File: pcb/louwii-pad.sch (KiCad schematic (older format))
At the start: 50 parts, among them J1 USB_B_Micro, J2 ICSP, J3 IIC, K1 KEYSW, K2 KEYSW, K3 KEYSW, K4 KEYSW, K5 KEYSW, K6 KEYSW, K7 KEYSW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

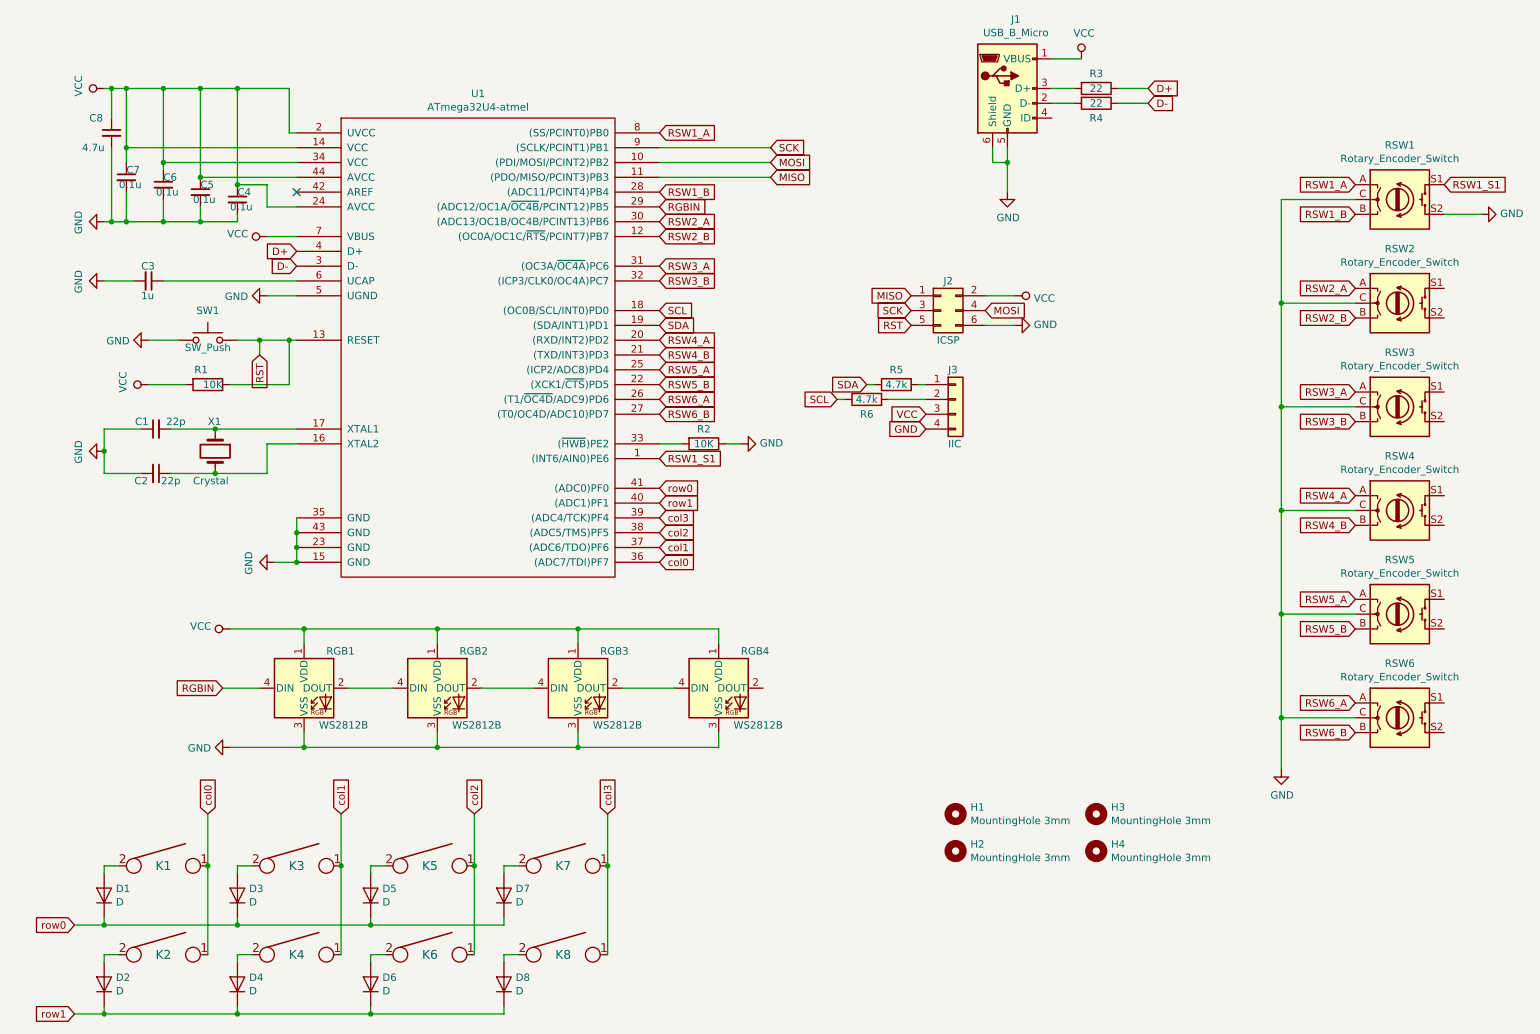
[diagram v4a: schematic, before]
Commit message: update schematics, update net, update footprints, update pcb design with missing footprints
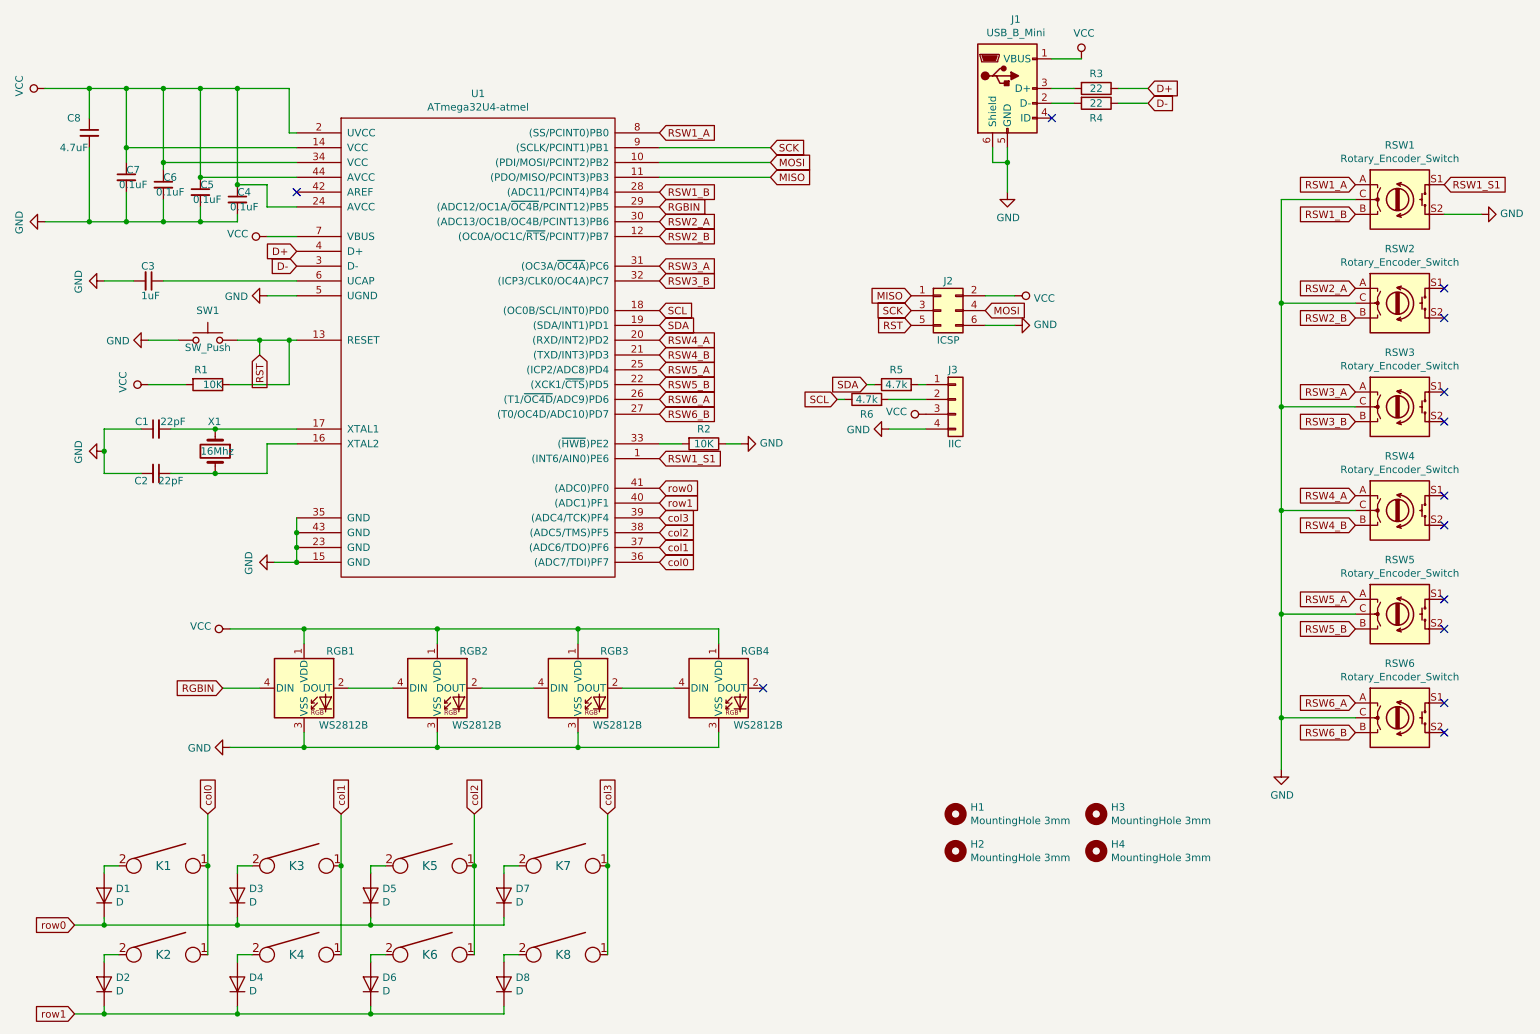
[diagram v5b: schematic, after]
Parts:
- removed J1: USB_B_Micro, Connector_USB:USB_Micro-B_Wuerth_629105150521, symbol Connector:USB_B_Micro
- added J1: USB_B_Mini, Connector_USB:USB_Mini-B_Lumberg_2486_01_Horizontal, symbol Connector:USB_B_Mini
- C1, C2: value 22p -> 22pF; footprint (none) -> Capacitor_THT:C_Disc_D4.3mm_W1.9mm_P5.00mm
- C3: value 1u -> 1uF; footprint (none) -> Capacitor_THT:C_Disc_D4.3mm_W1.9mm_P5.00mm
- C4, C5, C6, C7: value 0.1u -> 0.1uF; footprint (none) -> Capacitor_THT:C_Disc_D4.3mm_W1.9mm_P5.00mm
- C8: value 4.7u -> 4.7uF; footprint (none) -> Capacitor_THT:C_Radial_D5.0mm_H7.0mm_P2.00mm
- H1, H2, H3, H4: footprint (none) -> MountingHole:MountingHole_3.2mm_M3_ISO7380_Pad
- SW1: footprint (none) -> Button_Switch_SMD:SW_SPST_TL3342
- X1: value Crystal -> 16Mhz
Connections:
- net GND: now also J1.5 (GND), J1.6 (Shield)
- net VCC: now also J1.1 (VBUS)
- net at R4.2: now also J1.2 (D-)
- net at R3.2: now also J1.3 (D+)
- no-connect marks 1 -> 13
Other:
- moved on the sheet: C8
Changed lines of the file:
@@
 P 2050 3650
 F 0 "X1" V 1850 3600 50  0000 L CNN
-F 1 "Crystal" V 2250 3500 50  0000 L CNN
+F 1 "16Mhz" V 2050 3550 50  0000 L CNN
 F 2 "Crystal:Crystal_HC49-U_Vertical" H 2050 3650 50  0001 C CNN
 F 3 "~" H 2050 3650 50  0001 C CNN
@@
 P 1650 3800
 F 0 "C2" V 1700 3700 50  0000 C CNN
-F 1 "22p" V 1700 3900 50  0000 C CNN
-F 2 "" H 1650 3800 50  0001 C CNN
+F 1 "22pF" V 1700 3900 50  0000 C CNN
+F 2 "Capacitor_THT:C_Disc_D4.3mm_W1.9mm_P5.00mm" H 1650 3800 50  0001 C CNN
 F 3 "~" H 1650 3800 50  0001 C CNN
 	1    1650 3800
@@
 P 1650 3500
 F 0 "C1" V 1700 3550 50  0000 L CNN
-F 1 "22p" V 1700 3300 50  0000 L CNN
-F 2 "" H 1650 3500 50  0001 C CNN
+F 1 "22pF" V 1700 3300 50  0000 L CNN
+F 2 "Capacitor_THT:C_Disc_D4.3mm_W1.9mm_P5.00mm" H 1650 3500 50  0001 C CNN
 F 3 "~" H 1650 3500 50  0001 C CNN
 	1    1650 3500
 	0    -1   -1   0
-$EndComp
-$Comp
-L Connector:USB_B_Micro J1
-U 1 1 5DB104A8
-P 7400 1200
-F 0 "J1" H 7457 1667 50  0000 C CNN
-F 1 "USB_B_Micro" H 7457 1576 50  0000 C CNN
-F 2 "Connector_USB:USB_Micro-B_Wuerth_629105150521" H 7550 1150 50  0001 C CNN
-F 3 "~" H 7550 1150 50  0001 C CNN
-	1    7400 1200
-	1    0    0    -1
 $EndComp
 $Comp
@@
 P 1600 2500
 F 0 "C3" V 1500 2450 50  0000 L CNN
-F 1 "1u" V 1700 2450 50  0000 L CNN
-F 2 "" H 1600 2500 50  0001 C CNN
+F 1 "1uF" V 1700 2450 50  0000 L CNN
+F 2 "Capacitor_THT:C_Disc_D4.3mm_W1.9mm_P5.00mm" H 1600 2500 50  0001 C CNN
 F 3 "~" H 1600 2500 50  0001 C CNN
 	1    1600 2500
@@
 F 0 "SW1" H 2000 3100 50  0000 C CNN
 F 1 "SW_Push" H 2000 2850 50  0000 C CNN
-F 2 "" H 2000 3100 50  0001 C CNN
+F 2 "Button_Switch_SMD:SW_SPST_TL3342" H 2000 3100 50  0001 C CNN
 F 3 "~" H 2000 3100 50  0001 C CNN
 	1    2000 2900
@@
 P 2200 1950
 F 0 "C4" H 2200 2000 50  0000 L CNN
-F 1 "0.1u" H 2150 1900 50  0000 L CNN
-F 2 "" H 2200 1950 50  0001 C CNN
+F 1 "0.1uF" H 2150 1900 50  0000 L CNN
+F 2 "Capacitor_THT:C_Disc_D4.3mm_W1.9mm_P5.00mm" H 2200 1950 50  0001 C CNN
 F 3 "~" H 2200 1950 50  0001 C CNN
 	1    2200 1950
@@
 P 1950 1900
 F 0 "C5" H 1950 1950 50  0000 L CNN
-F 1 "0.1u" H 1900 1850 50  0000 L CNN
-F 2 "" H 1950 1900 50  0001 C CNN
+F 1 "0.1uF" H 1900 1850 50  0000 L CNN
+F 2 "Capacitor_THT:C_Disc_D4.3mm_W1.9mm_P5.00mm" H 1950 1900 50  0001 C CNN
 F 3 "~" H 1950 1900 50  0001 C CNN
 	1    1950 1900
@@
 P 1700 1850
 F 0 "C6" H 1700 1900 50  0000 L CNN
-F 1 "0.1u" H 1650 1800 50  0000 L CNN
-F 2 "" H 1700 1850 50  0001 C CNN
+F 1 "0.1uF" H 1650 1800 50  0000 L CNN
+F 2 "Capacitor_THT:C_Disc_D4.3mm_W1.9mm_P5.00mm" H 1700 1850 50  0001 C CNN
 F 3 "~" H 1700 1850 50  0001 C CNN
 	1    1700 1850
@@
 P 1450 1800
 F 0 "C7" H 1450 1850 50  0000 L CNN
-F 1 "0.1u" H 1400 1750 50  0000 L CNN
-F 2 "" H 1450 1800 50  0001 C CNN
+F 1 "0.1uF" H 1400 1750 50  0000 L CNN
+F 2 "Capacitor_THT:C_Disc_D4.3mm_W1.9mm_P5.00mm" H 1450 1800 50  0001 C CNN
 F 3 "~" H 1450 1800 50  0001 C CNN
 	1    1450 1800
@@
 L Device:C_Small C8
 U 1 1 5DB3CE28
-P 1350 1500
-F 0 "C8" H 1200 1600 50  0000 L CNN
-F 1 "4.7u" H 1150 1400 50  0000 L CNN
-F 2 "" H 1350 1500 50  0001 C CNN
-F 3 "~" H 1350 1500 50  0001 C CNN
-	1    1350 1500
+P 1200 1500
+F 0 "C8" H 1050 1600 50  0000 L CNN
+F 1 "4.7uF" H 1000 1400 50  0000 L CNN
+F 2 "Capacitor_THT:C_Radial_D5.0mm_H7.0mm_P2.00mm" H 1200 1500 50  0001 C CNN
+F 3 "~" H 1200 1500 50  0001 C CNN
+	1    1200 1500
 	1    0    0    -1
 $EndComp
@@
 L power:VCC #PWR0109
 U 1 1 5DB4ABC5
-P 1300 1200
-F 0 "#PWR0109" H 1300 1050 50  0001 C CNN
-F 1 "VCC" H 1317 1373 50  0000 C CNN
-F 2 "" H 1300 1200 50  0001 C CNN
-F 3 "" H 1300 1200 50  0001 C CNN
-	1    1300 1200
+P 900 1200
+F 0 "#PWR0109" H 900 1050 50  0001 C CNN
+F 1 "VCC" H 917 1373 50  0000 C CNN
+F 2 "" H 900 1200 50  0001 C CNN
+F 3 "" H 900 1200 50  0001 C CNN
+	1    900  1200
 	0    -1   -1   0
 $EndComp
@@
 L power:GND #PWR0112
 U 1 1 5DC49921
-P 1300 2100
-F 0 "#PWR0112" H 1300 1850 50  0001 C CNN
-F 1 "GND" H 1305 1927 50  0000 C CNN
-F 2 "" H 1300 2100 50  0001 C CNN
-F 3 "" H 1300 2100 50  0001 C CNN
-	1    1300 2100
+P 900 2100
+F 0 "#PWR0112" H 900 1850 50  0001 C CNN
+F 1 "GND" H 905 1927 50  0000 C CNN
+F 2 "" H 900 2100 50  0001 C CNN
+F 3 "" H 900 2100 50  0001 C CNN
+	1    900  2100
 	0    1    1    0
 $EndComp
@@
 Connection ~ 1700 1200
 Wire Wire Line
-	1300 1200 1350 1200
-Wire Wire Line
 	1450 1600 1450 1200
 Wire Wire Line
@@
 	1450 1200 1700 1200
 Wire Wire Line
-	1300 2100 1350 2100
-Wire Wire Line
-	1350 1400 1350 1200
-Connection ~ 1350 1200
-Wire Wire Line
-	1350 1200 1450 1200
-Connection ~ 1350 2100
-Wire Wire Line
-	1350 2100 1450 2100
-Wire Wire Line
-	1350 1600 1350 2100
+	1200 1400 1200 1200
+Wire Wire Line
+	1200 1600 1200 2100
 Wire Wire Line
 	1450 1600 1450 1700
@@
 Text GLabel 6250 3300 0    50   Input ~ 0
 SCL
-Text GLabel 6850 3400 0    50   Input ~ 0
-VCC
-Text GLabel 6850 3500 0    50   Input ~ 0
-GND
 Wire Wire Line
 	5800 1600 5050 1600
@@
 F 0 "H2" H 7150 6396 50  0000 L CNN
 F 1 "MountingHole 3mm" H 7150 6305 50  0000 L CNN
-F 2 "" H 7050 6350 50  0001 C CNN
+F 2 "MountingHole:MountingHole_3.2mm_M3_ISO7380_Pad" H 7050 6350 50  0001 C CNN
 F 3 "~" H 7050 6350 50  0001 C CNN
 	1    7050 6350
@@
 F 0 "H1" H 7150 6146 50  0000 L CNN
 F 1 "MountingHole 3mm" H 7150 6055 50  0000 L CNN
-F 2 "" H 7050 6100 50  0001 C CNN
+F 2 "MountingHole:MountingHole_3.2mm_M3_ISO7380_Pad" H 7050 6100 50  0001 C CNN
 F 3 "~" H 7050 6100 50  0001 C CNN
 	1    7050 6100
@@
 F 0 "H3" H 8100 6146 50  0000 L CNN
 F 1 "MountingHole 3mm" H 8100 6055 50  0000 L CNN
-F 2 "" H 8000 6100 50  0001 C CNN
+F 2 "MountingHole:MountingHole_3.2mm_M3_ISO7380_Pad" H 8000 6100 50  0001 C CNN
 F 3 "~" H 8000 6100 50  0001 C CNN
 	1    8000 6100
@@
 F 0 "H4" H 8100 6396 50  0000 L CNN
 F 1 "MountingHole 3mm" H 8100 6305 50  0000 L CNN
-F 2 "" H 8000 6350 50  0001 C CNN
+F 2 "MountingHole:MountingHole_3.2mm_M3_ISO7380_Pad" H 8000 6350 50  0001 C CNN
 F 3 "~" H 8000 6350 50  0001 C CNN
 	1    8000 6350
@@
 Wire Wire Line
 	2350 5250 2100 5250
+$Comp
+L Connector:USB_B_Mini J1
+U 1 1 5DB46E94
+P 7400 1200
+F 0 "J1" H 7457 1667 50  0000 C CNN
+F 1 "USB_B_Mini" H 7457 1576 50  0000 C CNN
+F 2 "Connector_USB:USB_Mini-B_Lumberg_2486_01_Horizontal" H 7550 1150 50  0001 C CNN
+F 3 "~" H 7550 1150 50  0001 C CNN
+	1    7400 1200
+	1    0    0    -1
+$EndComp
+NoConn ~ 10350 2550
+NoConn ~ 10350 2750
+NoConn ~ 10350 3250
+NoConn ~ 10350 3450
+NoConn ~ 10350 3950
+NoConn ~ 10350 4150
+NoConn ~ 10350 4650
+NoConn ~ 10350 4850
+NoConn ~ 10350 5350
+NoConn ~ 10350 5550
+NoConn ~ 7700 1400
+NoConn ~ 5750 5250
+$Comp
+L power:GND #PWR0119
+U 1 1 5DBA983F
+P 6600 3500
+F 0 "#PWR0119" H 6600 3250 50  0001 C CNN
+F 1 "GND" V 6605 3372 50  0000 R CNN
+F 2 "" H 6600 3500 50  0001 C CNN
+F 3 "" H 6600 3500 50  0001 C CNN
+	1    6600 3500
+	0    1    1    0
+$EndComp
+Wire Wire Line
+	6850 3500 6600 3500
+$Comp
+L power:VCC #PWR0120
+U 1 1 5DBBD9B3
+P 6850 3400
+F 0 "#PWR0120" H 6850 3250 50  0001 C CNN
+F 1 "VCC" V 6867 3528 50  0000 L CNN
+F 2 "" H 6850 3400 50  0001 C CNN
+F 3 "" H 6850 3400 50  0001 C CNN
+	1    6850 3400
+	0    -1   -1   0
+$EndComp
+Wire Wire Line
+	900  1200 1200 1200
+Connection ~ 1200 1200
+Wire Wire Line
+	1200 1200 1450 1200
+Wire Wire Line
+	900  2100 1200 2100
+Connection ~ 1200 2100
+Wire Wire Line
+	1200 2100 1450 2100
 $EndSCHEMATC

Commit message: add more 3d models, finish up PCB tracing
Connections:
- net RSW1_A: now also U1.26 ((T1/~OC4D~/ADC9)PD6); no longer U1.8 ((SS/PCINT0)PB0)
- net RSW1_B: now also U1.25 ((ICP2/ADC8)PD4); no longer U1.28 ((ADC11/PCINT4)PB4)
- net RSW1_S1: now also U1.22 ((XCK1/~CTS~)PD5); no longer U1.1 ((INT6/AIN0)PE6)
- net RSW2_A: now also U1.37 ((ADC6/TDO)PF6); no longer U1.30 ((ADC13/OC1B/OC4B/PCINT13)PB6)
- net RSW2_B: now also U1.36 ((ADC7/TDI)PF7); no longer U1.12 ((OC0A/OC1C/~RTS~/PCINT7)PB7)
- net RSW3_A: now also U1.20 ((RXD/INT2)PD2); no longer U1.31 ((OC3A/~OC4A~)PC6)
- net RSW3_B: now also U1.21 ((TXD/INT3)PD3); no longer U1.32 ((ICP3/CLK0/OC4A)PC7)
- net RSW4_A: now also U1.40 ((ADC1)PF1); no longer U1.20 ((RXD/INT2)PD2)
- net RSW4_B: now also U1.39 ((ADC4/TCK)PF4); no longer U1.21 ((TXD/INT3)PD3)
- net RSW5_A: now also U1.12 ((OC0A/OC1C/~RTS~/PCINT7)PB7); no longer U1.25 ((ICP2/ADC8)PD4)
- net RSW5_B: now also U1.8 ((SS/PCINT0)PB0); no longer U1.22 ((XCK1/~CTS~)PD5)
- net RSW6_A: now also U1.1 ((INT6/AIN0)PE6); no longer U1.26 ((T1/~OC4D~/ADC9)PD6)
- net RSW6_B: now also U1.41 ((ADC0)PF0); no longer U1.27 ((T0/OC4D/ADC10)PD7)
- net col0: now also U1.30 ((ADC13/OC1B/OC4B/PCINT13)PB6); no longer U1.36 ((ADC7/TDI)PF7)
- net col1: now also U1.31 ((OC3A/~OC4A~)PC6); no longer U1.37 ((ADC6/TDO)PF6)
- net col2: now also U1.32 ((ICP3/CLK0/OC4A)PC7); no longer U1.38 ((ADC5/TMS)PF5)
- net col3: now also U1.38 ((ADC5/TMS)PF5); no longer U1.39 ((ADC4/TCK)PF4)
- net row0: now also U1.27 ((T0/OC4D/ADC10)PD7); no longer U1.41 ((ADC0)PF0)
- net row1: now also U1.28 ((ADC11/PCINT4)PB4); no longer U1.40 ((ADC1)PF1)
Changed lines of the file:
@@
 	1    0    0    -1
 $EndComp
-Text GLabel 5050 1500 2    50   Input ~ 0
+Text GLabel 5050 3300 2    50   Input ~ 0
 RSW1_A
-Text GLabel 5050 1900 2    50   Input ~ 0
+Text GLabel 5050 3100 2    50   Input ~ 0
 RSW1_B
 Text GLabel 9750 1850 0    50   Input ~ 0
@@
 Text GLabel 9750 2050 0    50   Input ~ 0
 RSW1_B
-Text GLabel 5050 2100 2    50   Input ~ 0
+Text GLabel 5050 4300 2    50   Input ~ 0
 RSW2_A
-Text GLabel 5050 2200 2    50   Input ~ 0
+Text GLabel 5050 4400 2    50   Input ~ 0
 RSW2_B
-Text GLabel 5050 2400 2    50   Input ~ 0
+Text GLabel 5050 2900 2    50   Input ~ 0
 RSW3_A
-Text GLabel 5050 2500 2    50   Input ~ 0
+Text GLabel 5050 3000 2    50   Input ~ 0
 RSW3_B
-Text GLabel 5050 2900 2    50   Input ~ 0
+Text GLabel 5050 4000 2    50   Input ~ 0
 RSW4_A
-Text GLabel 5050 3000 2    50   Input ~ 0
+Text GLabel 5050 4100 2    50   Input ~ 0
 RSW4_B
 Connection ~ 9250 4050
@@
 Text GLabel 9750 4850 0    50   Input ~ 0
 RSW5_B
-Text GLabel 5050 3100 2    50   Input ~ 0
+Text GLabel 5050 2200 2    50   Input ~ 0
 RSW5_A
-Text GLabel 5050 3200 2    50   Input ~ 0
+Text GLabel 5050 1500 2    50   Input ~ 0
 RSW5_B
 Wire Wire Line
@@
 Text GLabel 9750 5550 0    50   Input ~ 0
 RSW6_B
-Text GLabel 5050 3300 2    50   Input ~ 0
+Text GLabel 5050 3700 2    50   Input ~ 0
 RSW6_A
-Text GLabel 5050 3400 2    50   Input ~ 0
+Text GLabel 5050 3900 2    50   Input ~ 0
 RSW6_B
 $Comp
@@
 	2000 6450 2000 6100
 Connection ~ 2000 6450
-Text GLabel 5050 3900 2    50   Input ~ 0
+Text GLabel 5050 3400 2    50   Input ~ 0
 row0
-Text GLabel 5050 4000 2    50   Input ~ 0
+Text GLabel 5050 1900 2    50   Input ~ 0
 row1
-Text GLabel 5050 4400 2    50   Input ~ 0
+Text GLabel 5050 2100 2    50   Input ~ 0
 col0
+Text GLabel 5050 2500 2    50   Input ~ 0
+col2
+Text GLabel 5050 2400 2    50   Input ~ 0
+col1
 Text GLabel 5050 4200 2    50   Input ~ 0
-col2
-Text GLabel 5050 4300 2    50   Input ~ 0
-col1
-Text GLabel 5050 4100 2    50   Input ~ 0
 col3
 Text GLabel 5050 2700 2    50   Input ~ 0
@@
 Wire Wire Line
 	10600 2050 10350 2050
-Text GLabel 5050 3700 2    50   Input ~ 0
+Text GLabel 5050 3200 2    50   Input ~ 0
 RSW1_S1
 $Comp

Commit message: finish up tracing, updating footprints, adding 3d models
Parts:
- RGB1, RGB2, RGB3, RGB4: footprint LED_SMD:LED_WS2812B_PLCC4_5.0x5.0mm_P3.2mm -> keyboard_parts:WS2812b
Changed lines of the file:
@@
 F 0 "RGB1" H 2800 5500 50  0000 L CNN
 F 1 "WS2812B" H 2750 5000 50  0000 L CNN
-F 2 "LED_SMD:LED_WS2812B_PLCC4_5.0x5.0mm_P3.2mm" H 2700 4950 50  0001 L TNN
+F 2 "keyboard_parts:WS2812b" H 2700 4950 50  0001 L TNN
 F 3 "https://cdn-shop.adafruit.com/datasheets/WS2812B.pdf" H 2750 4875 50  0001 L TNN
 	1    2650 5250
@@
 F 0 "RGB2" H 3700 5500 50  0000 L CNN
 F 1 "WS2812B" H 3650 5000 50  0000 L CNN
-F 2 "LED_SMD:LED_WS2812B_PLCC4_5.0x5.0mm_P3.2mm" H 3600 4950 50  0001 L TNN
+F 2 "keyboard_parts:WS2812b" H 3600 4950 50  0001 L TNN
 F 3 "https://cdn-shop.adafruit.com/datasheets/WS2812B.pdf" H 3650 4875 50  0001 L TNN
 	1    3550 5250
@@
 F 0 "RGB3" H 4650 5500 50  0000 L CNN
 F 1 "WS2812B" H 4600 5000 50  0000 L CNN
-F 2 "LED_SMD:LED_WS2812B_PLCC4_5.0x5.0mm_P3.2mm" H 4550 4950 50  0001 L TNN
+F 2 "keyboard_parts:WS2812b" H 4550 4950 50  0001 L TNN
 F 3 "https://cdn-shop.adafruit.com/datasheets/WS2812B.pdf" H 4600 4875 50  0001 L TNN
 	1    4500 5250
@@
 F 0 "RGB4" H 5600 5500 50  0000 L CNN
 F 1 "WS2812B" H 5550 5000 50  0000 L CNN
-F 2 "LED_SMD:LED_WS2812B_PLCC4_5.0x5.0mm_P3.2mm" H 5500 4950 50  0001 L TNN
+F 2 "keyboard_parts:WS2812b" H 5500 4950 50  0001 L TNN
 F 3 "https://cdn-shop.adafruit.com/datasheets/WS2812B.pdf" H 5550 4875 50  0001 L TNN
 	1    5450 5250
